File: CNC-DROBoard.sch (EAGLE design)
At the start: 50 parts, among them IC1 ATTINY2313A-PU, IC2 MAX7219CNG, IC3 MAX7219CNG, IC4 74HCT4053P

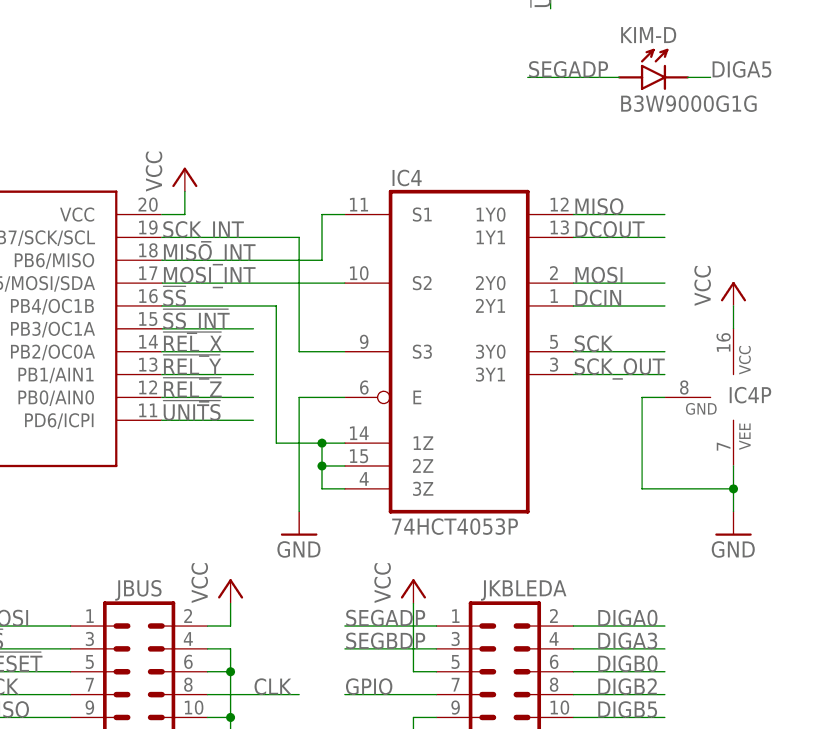
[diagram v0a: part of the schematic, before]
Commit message: BUGFIX: 74LS4053 doesn't have the commons where you'd think it has - misleading symbol helped me mistake select inputs for common outputs - updated schematic, PCB update pending - this is probably not reworkable on a populated PCB. Will investigate reworkability of a blank PCB - contingency: dead-bug tehnique for the 4053 and onwards we go.
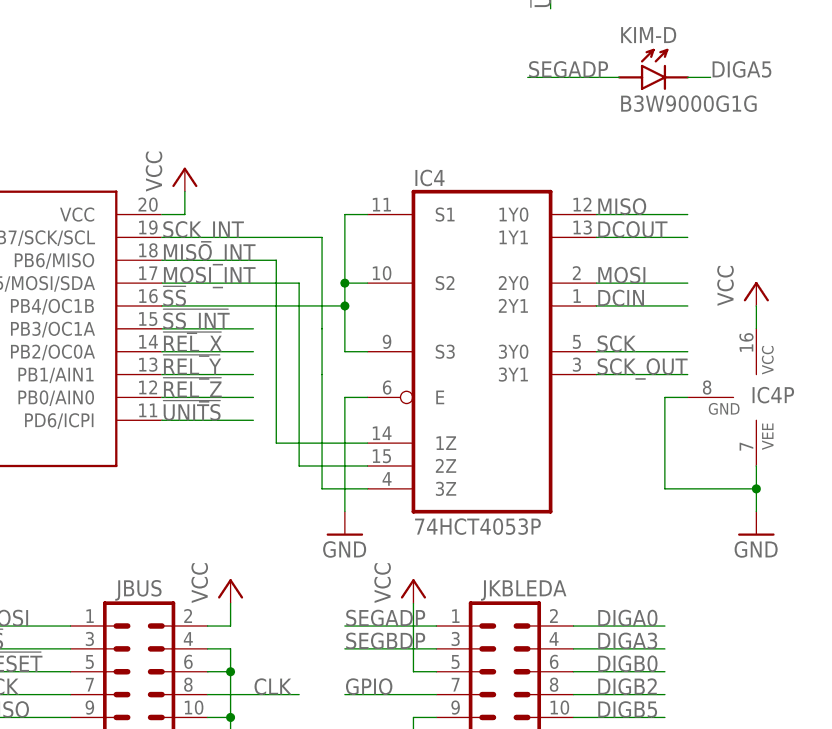
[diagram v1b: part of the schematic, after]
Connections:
- net !SS: now also IC4G$1.S1, IC4G$1.S2, IC4G$1.S3; no longer IC4G$1.1Z, IC4G$1.2Z, IC4G$1.3Z
- net MISO_INT: now also IC4G$1.1Z; no longer IC4G$1.S1
- net MOSI_INT: now also IC4G$1.2Z; no longer IC4G$1.S2
- net SCK_INT: now also IC4G$1.3Z; no longer IC4G$1.S3
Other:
- moved on the sheet: IC4, IC4P
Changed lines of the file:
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@@
 <?xml version="1.0" encoding="utf-8"?>
 <!DOCTYPE eagle SYSTEM "eagle.dtd">
-<eagle version="6.3">
+<eagle version="6.4">
 <drawing>
 <settings>
@@
 <instance part="P+2" gate="VCC" x="358.14" y="43.18"/>
 <instance part="GND18" gate="1" x="358.14" y="22.86"/>
-<instance part="IC4" gate="G$1" x="363.22" y="68.58"/>
-<instance part="IC4" gate="P" x="393.7" y="63.5"/>
-<instance part="GND19" gate="1" x="393.7" y="48.26"/>
-<instance part="+5V6" gate="VCC" x="393.7" y="76.2"/>
-<instance part="GND15" gate="1" x="345.44" y="48.26"/>
+<instance part="IC4" gate="G$1" x="365.76" y="68.58"/>
+<instance part="IC4" gate="P" x="396.24" y="63.5"/>
+<instance part="GND19" gate="1" x="396.24" y="48.26"/>
+<instance part="+5V6" gate="VCC" x="396.24" y="76.2"/>
+<instance part="GND15" gate="1" x="350.52" y="48.26"/>
 <instance part="U$1" gate="G$1" x="358.14" y="152.4"/>
 </instances>
@@
 <pinref part="IC4" gate="P" pin="VEE"/>
 <pinref part="GND19" gate="1" pin="GND"/>
-<wire x1="393.7" y1="55.88" x2="393.7" y2="53.34" width="0.1524" layer="91"/>
+<wire x1="396.24" y1="55.88" x2="396.24" y2="53.34" width="0.1524" layer="91"/>
 <pinref part="IC4" gate="P" pin="GND"/>
-<wire x1="393.7" y1="53.34" x2="393.7" y2="50.8" width="0.1524" layer="91"/>
-<wire x1="386.08" y1="63.5" x2="383.54" y2="63.5" width="0.1524" layer="91"/>
-<wire x1="383.54" y1="63.5" x2="383.54" y2="53.34" width="0.1524" layer="91"/>
-<wire x1="383.54" y1="53.34" x2="393.7" y2="53.34" width="0.1524" layer="91"/>
-<junction x="393.7" y="53.34"/>
+<wire x1="396.24" y1="53.34" x2="396.24" y2="50.8" width="0.1524" layer="91"/>
+<wire x1="388.62" y1="63.5" x2="386.08" y2="63.5" width="0.1524" layer="91"/>
+<wire x1="386.08" y1="63.5" x2="386.08" y2="53.34" width="0.1524" layer="91"/>
+<wire x1="386.08" y1="53.34" x2="396.24" y2="53.34" width="0.1524" layer="91"/>
+<junction x="396.24" y="53.34"/>
 </segment>
 <segment>
 <pinref part="IC4" gate="G$1" pin="E"/>
 <pinref part="GND15" gate="1" pin="GND"/>
-<wire x1="350.52" y1="63.5" x2="345.44" y2="63.5" width="0.1524" layer="91"/>
-<wire x1="345.44" y1="63.5" x2="345.44" y2="50.8" width="0.1524" layer="91"/>
+<wire x1="353.06" y1="63.5" x2="350.52" y2="63.5" width="0.1524" layer="91"/>
+<wire x1="350.52" y1="63.5" x2="350.52" y2="50.8" width="0.1524" layer="91"/>
 </segment>
 </net>
@@
 <segment>
 <pinref part="IC4" gate="G$1" pin="2Y0"/>
-<wire x1="375.92" y1="76.2" x2="386.08" y2="76.2" width="0.1524" layer="91"/>
-<label x="375.92" y="76.2" size="1.778" layer="95"/>
+<wire x1="378.46" y1="76.2" x2="388.62" y2="76.2" width="0.1524" layer="91"/>
+<label x="378.46" y="76.2" size="1.778" layer="95"/>
 </segment>
 </net>
@@
 <segment>
 <pinref part="IC4" gate="G$1" pin="3Y0"/>
-<wire x1="375.92" y1="68.58" x2="386.08" y2="68.58" width="0.1524" layer="91"/>
-<label x="375.92" y="68.58" size="1.778" layer="95"/>
+<wire x1="378.46" y1="68.58" x2="388.62" y2="68.58" width="0.1524" layer="91"/>
+<label x="378.46" y="68.58" size="1.778" layer="95"/>
 </segment>
 </net>
@@
 <pinref part="+5V6" gate="VCC" pin="VCC"/>
 <pinref part="IC4" gate="P" pin="VCC"/>
-<wire x1="393.7" y1="73.66" x2="393.7" y2="71.12" width="0.1524" layer="91"/>
+<wire x1="396.24" y1="73.66" x2="396.24" y2="71.12" width="0.1524" layer="91"/>
 </segment>
 </net>
@@
 <segment>
 <pinref part="IC4" gate="G$1" pin="1Y0"/>
-<wire x1="375.92" y1="83.82" x2="386.08" y2="83.82" width="0.1524" layer="91"/>
-<label x="375.92" y="83.82" size="1.778" layer="95"/>
+<wire x1="378.46" y1="83.82" x2="388.62" y2="83.82" width="0.1524" layer="91"/>
+<label x="378.46" y="83.82" size="1.778" layer="95"/>
 </segment>
 </net>
@@
 <pinref part="IC1" gate="A" pin="PB4/OC1B"/>
 <label x="330.2" y="73.66" size="1.778" layer="95"/>
-<wire x1="330.2" y1="73.66" x2="342.9" y2="73.66" width="0.1524" layer="91"/>
-<wire x1="342.9" y1="73.66" x2="342.9" y2="58.42" width="0.1524" layer="91"/>
-<pinref part="IC4" gate="G$1" pin="1Z"/>
-<wire x1="342.9" y1="58.42" x2="347.98" y2="58.42" width="0.1524" layer="91"/>
-<wire x1="347.98" y1="58.42" x2="350.52" y2="58.42" width="0.1524" layer="91"/>
-<wire x1="347.98" y1="58.42" x2="347.98" y2="55.88" width="0.1524" layer="91"/>
-<junction x="347.98" y="58.42"/>
-<pinref part="IC4" gate="G$1" pin="2Z"/>
-<wire x1="347.98" y1="55.88" x2="350.52" y2="55.88" width="0.1524" layer="91"/>
-<wire x1="347.98" y1="55.88" x2="347.98" y2="53.34" width="0.1524" layer="91"/>
-<junction x="347.98" y="55.88"/>
-<pinref part="IC4" gate="G$1" pin="3Z"/>
-<wire x1="347.98" y1="53.34" x2="350.52" y2="53.34" width="0.1524" layer="91"/>
+<wire x1="330.2" y1="73.66" x2="350.52" y2="73.66" width="0.1524" layer="91"/>
+<wire x1="350.52" y1="73.66" x2="350.52" y2="68.58" width="0.1524" layer="91"/>
+<pinref part="IC4" gate="G$1" pin="S3"/>
+<wire x1="353.06" y1="68.58" x2="350.52" y2="68.58" width="0.1524" layer="91"/>
+<pinref part="IC4" gate="G$1" pin="S2"/>
+<wire x1="353.06" y1="76.2" x2="350.52" y2="76.2" width="0.1524" layer="91"/>
+<wire x1="350.52" y1="76.2" x2="350.52" y2="73.66" width="0.1524" layer="91"/>
+<junction x="350.52" y="73.66"/>
+<pinref part="IC4" gate="G$1" pin="S1"/>
+<wire x1="353.06" y1="83.82" x2="350.52" y2="83.82" width="0.1524" layer="91"/>
+<wire x1="350.52" y1="83.82" x2="350.52" y2="76.2" width="0.1524" layer="91"/>
+<junction x="350.52" y="76.2"/>
 </segment>
 </net>
@@
 <pinref part="IC1" gate="A" pin="PB7/SCK/SCL"/>
 <label x="330.2" y="81.28" size="1.778" layer="95"/>
-<wire x1="330.2" y1="81.28" x2="345.44" y2="81.28" width="0.1524" layer="91"/>
-<wire x1="345.44" y1="81.28" x2="345.44" y2="68.58" width="0.1524" layer="91"/>
-<pinref part="IC4" gate="G$1" pin="S3"/>
-<wire x1="345.44" y1="68.58" x2="350.52" y2="68.58" width="0.1524" layer="91"/>
-</segment>
-</net>
-<net name="MOSI_INT" class="0">
-<segment>
-<pinref part="IC1" gate="A" pin="PB5/MOSI/SDA"/>
-<label x="330.2" y="76.2" size="1.778" layer="95"/>
-<pinref part="IC4" gate="G$1" pin="S2"/>
-<wire x1="330.2" y1="76.2" x2="350.52" y2="76.2" width="0.1524" layer="91"/>
+<wire x1="330.2" y1="81.28" x2="347.98" y2="81.28" width="0.1524" layer="91"/>
+<wire x1="347.98" y1="81.28" x2="347.98" y2="71.12" width="0.1524" layer="91"/>
+<pinref part="IC4" gate="G$1" pin="3Z"/>
+<wire x1="353.06" y1="53.34" x2="347.98" y2="53.34" width="0.1524" layer="91"/>
+<wire x1="347.98" y1="53.34" x2="347.98" y2="66.04" width="0.1524" layer="91"/>
+<wire x1="347.98" y1="66.04" x2="347.98" y2="71.12" width="0.1524" layer="91"/>
 </segment>
 </net>
@@
 <segment>
 <pinref part="IC4" gate="G$1" pin="2Y1"/>
-<wire x1="375.92" y1="73.66" x2="386.08" y2="73.66" width="0.1524" layer="91"/>
-<label x="375.92" y="73.66" size="1.778" layer="95"/>
+<wire x1="378.46" y1="73.66" x2="388.62" y2="73.66" width="0.1524" layer="91"/>
+<label x="378.46" y="73.66" size="1.778" layer="95"/>
 </segment>
 </net>
@@
 <segment>
 <pinref part="IC4" gate="G$1" pin="3Y1"/>
-<wire x1="375.92" y1="66.04" x2="386.08" y2="66.04" width="0.1524" layer="91"/>
-<label x="375.92" y="66.04" size="1.778" layer="95"/>
+<wire x1="378.46" y1="66.04" x2="388.62" y2="66.04" width="0.1524" layer="91"/>
+<label x="378.46" y="66.04" size="1.778" layer="95"/>
 </segment>
 </net>
@@
 <pinref part="IC1" gate="A" pin="PB6/MISO"/>
 <label x="330.2" y="78.74" size="1.778" layer="95"/>
-<wire x1="330.2" y1="78.74" x2="347.98" y2="78.74" width="0.1524" layer="91"/>
-<wire x1="347.98" y1="78.74" x2="347.98" y2="83.82" width="0.1524" layer="91"/>
-<pinref part="IC4" gate="G$1" pin="S1"/>
-<wire x1="347.98" y1="83.82" x2="350.52" y2="83.82" width="0.1524" layer="91"/>
+<wire x1="330.2" y1="78.74" x2="342.9" y2="78.74" width="0.1524" layer="91"/>
+<wire x1="342.9" y1="78.74" x2="342.9" y2="58.42" width="0.1524" layer="91"/>
+<pinref part="IC4" gate="G$1" pin="1Z"/>
+<wire x1="342.9" y1="58.42" x2="353.06" y2="58.42" width="0.1524" layer="91"/>
 </segment>
 </net>
@@
 <segment>
 <pinref part="IC4" gate="G$1" pin="1Y1"/>
-<wire x1="375.92" y1="81.28" x2="386.08" y2="81.28" width="0.1524" layer="91"/>
-<label x="375.92" y="81.28" size="1.778" layer="95"/>
-</segment>
-</net>
+<wire x1="378.46" y1="81.28" x2="388.62" y2="81.28" width="0.1524" layer="91"/>
+<label x="378.46" y="81.28" size="1.778" layer="95"/>
+</segment>
+</net>
+<net name="MOSI_INT" class="0">
+<segment>
+<pinref part="IC4" gate="G$1" pin="2Z"/>
+<wire x1="353.06" y1="55.88" x2="345.44" y2="55.88" width="0.1524" layer="91"/>
+<wire x1="345.44" y1="55.88" x2="345.44" y2="76.2" width="0.1524" layer="91"/>
+<pinref part="IC1" gate="A" pin="PB5/MOSI/SDA"/>
+<wire x1="345.44" y1="76.2" x2="330.2" y2="76.2" width="0.1524" layer="91"/>
+<label x="330.2" y="76.2" size="1.778" layer="95"/>
+</segment>
+</net>

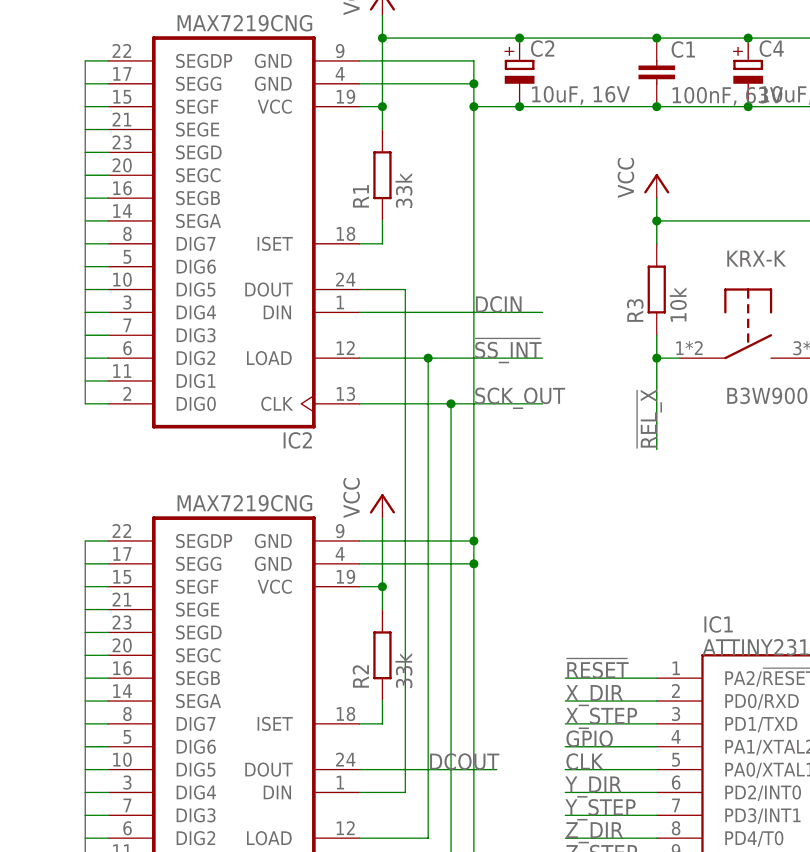
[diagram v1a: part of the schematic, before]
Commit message: BUGFIX: Same 4053 mistake fixed on Controls board as well UPDATE: 27k instead of 33k for Riset as all LEDs can handle 20mA at 2.1V - routed both DRO and Controls in FreeRouting - updated silkscreen/artwork to reflect new revision - still needs to fix DRU checks (FreeRouting always sees non-PTH holes smaller)
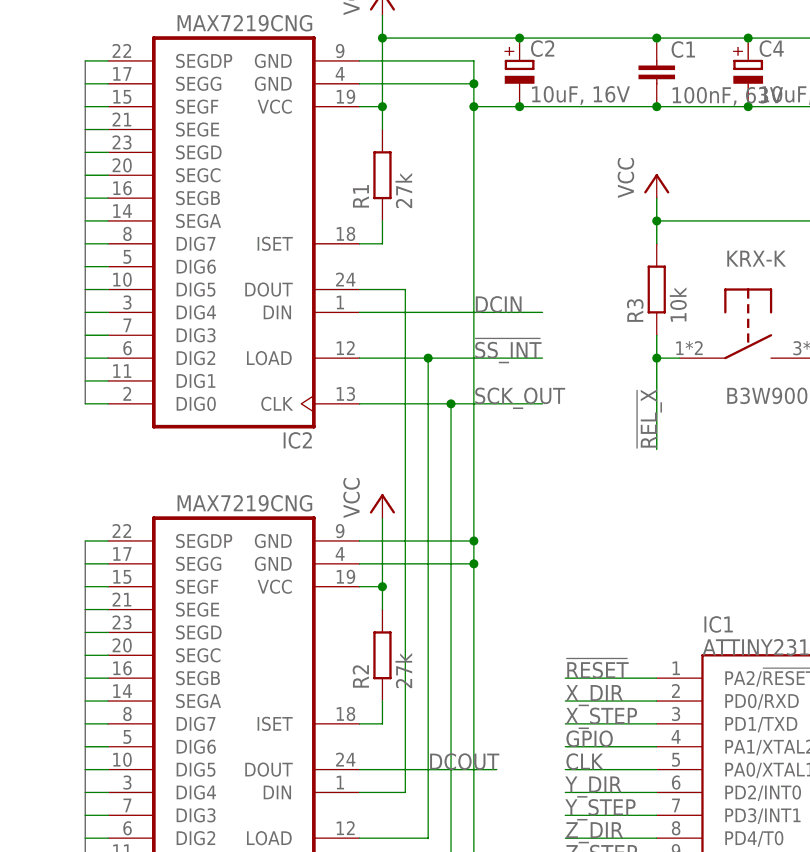
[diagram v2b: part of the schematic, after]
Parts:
- R1, R2: value 33k -> 27k
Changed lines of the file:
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@@
 <part name="IC2" library="maxim" deviceset="MAX7219CNG" device=""/>
 <part name="IC3" library="maxim" deviceset="MAX7219CNG" device=""/>
-<part name="R1" library="rcl" deviceset="R-EU_" device="0207/10" value="33k"/>
-<part name="R2" library="rcl" deviceset="R-EU_" device="0207/10" value="33k"/>
+<part name="R1" library="rcl" deviceset="R-EU_" device="0207/10" value="27k"/>
+<part name="R2" library="rcl" deviceset="R-EU_" device="0207/10" value="27k"/>
 <part name="+5V" library="supply1" deviceset="VCC" device=""/>
 <part name="+5V1" library="supply1" deviceset="VCC" device=""/>
